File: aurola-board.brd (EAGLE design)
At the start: 86.4 x 31.8 mm, 84 parts, among them IC1 STM32F051C6T, J1 CONN_PWM, J2 CONN_TEMP, J3 CONN_FAN, J4 CONN_EC11, J5 CONN_I2C, P1 KF128-2P, Q1 600mA/40V, U1 ESP-01F, U2 BL9341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

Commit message: 完成布局
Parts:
- moved C16 0.63 mm to (30.4, 5.71)
- moved C14 0.51 mm to (30.4, 11.6)
- moved C13 0.51 mm to (30.4, 8.13)
- moved U$1 0.51 mm to (27.2, 8.00)
- moved U$2 0.38 mm to (27.2, 3.17)
- moved C15 0.25 mm to (30.4, 3.30)
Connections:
- removed net N$26: C28.+, D3.C, D4.P$1, F1.1
- new net EC_INT: IC1.42, U1.6
- net FAN_SPEED: now also IC1.13
- net VIN: now also C28.+, D3.C, D4.P$1, F1.1
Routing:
- net 3.3V: track 0.00 -> 173.9 mm, vias 0 -> 4
- net GND: track 0.00 -> 94.0 mm, vias 0 -> 78
- net FAN_SPEED: track 0.00 -> 56.4 mm, vias 0 -> 2
- net SDA: track 0.00 -> 55.6 mm, vias 0 -> 3
- net SCL: track 0.00 -> 54.7 mm, vias 0 -> 3
- net FAN_PWM: track 0.00 -> 51.1 mm, vias 0 -> 2
- net VIN: track 0.00 -> 50.7 mm, vias 0 -> 2
- net EC_INT: track 0.00 -> 47.9 mm, vias 0 -> 2
- net 12V: track 0.00 -> 37.1 mm, vias 0 -> 3
- net EC_A: track 0.00 -> 33.6 mm, vias 0 -> 2
- net RST: track 0.00 -> 30.7 mm, vias 0 -> 2
- net EC_B: track 0.00 -> 30.2 mm, vias 0 -> 2
- net EC_SW: track 0.00 -> 23.1 mm
- net TEMP_DO: track 0.00 -> 18.8 mm
- net TX: track 0.00 -> 18.8 mm
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- added copper zone on layer 1, net GND
- added copper zone on layer 16, net GND
- added copper zone on layer 1, net N$2
- added copper zone on layer 1, net N$6
- added copper zone on layer 1, net VIN

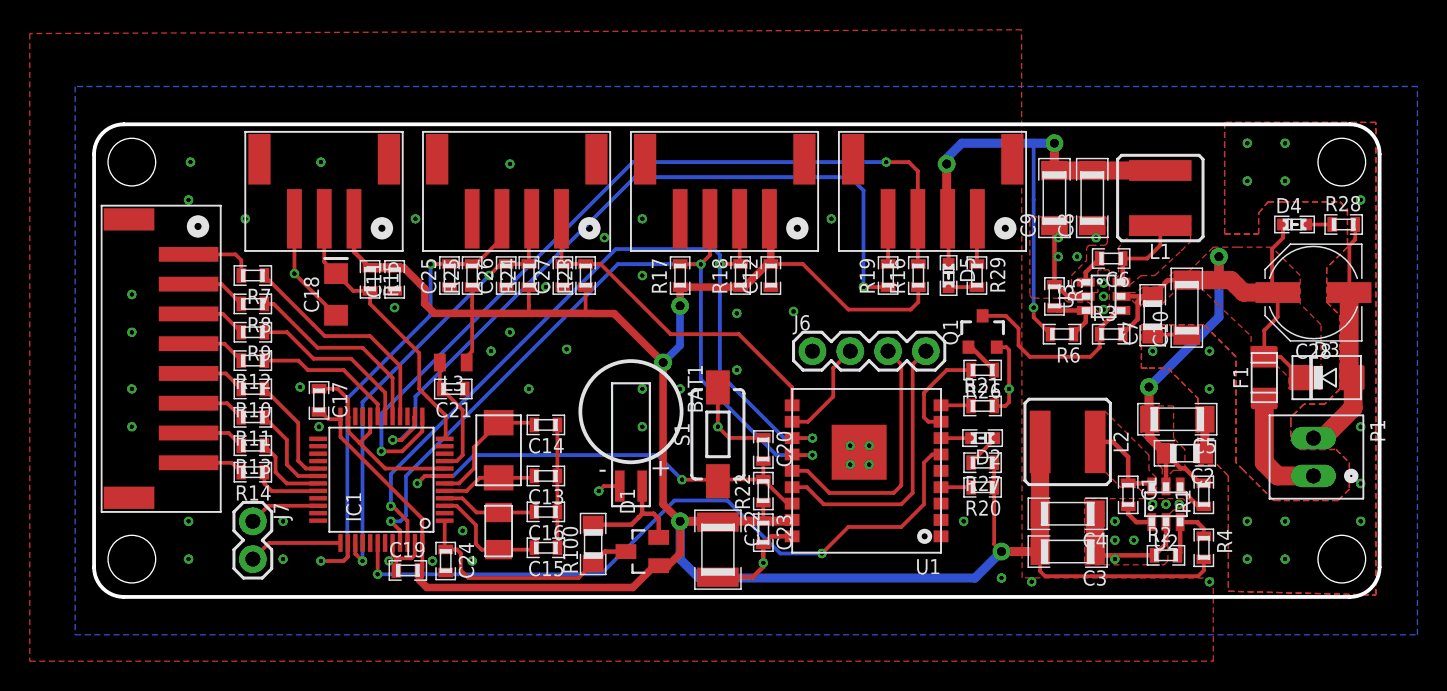
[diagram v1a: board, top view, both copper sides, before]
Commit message: 调整丝印位置
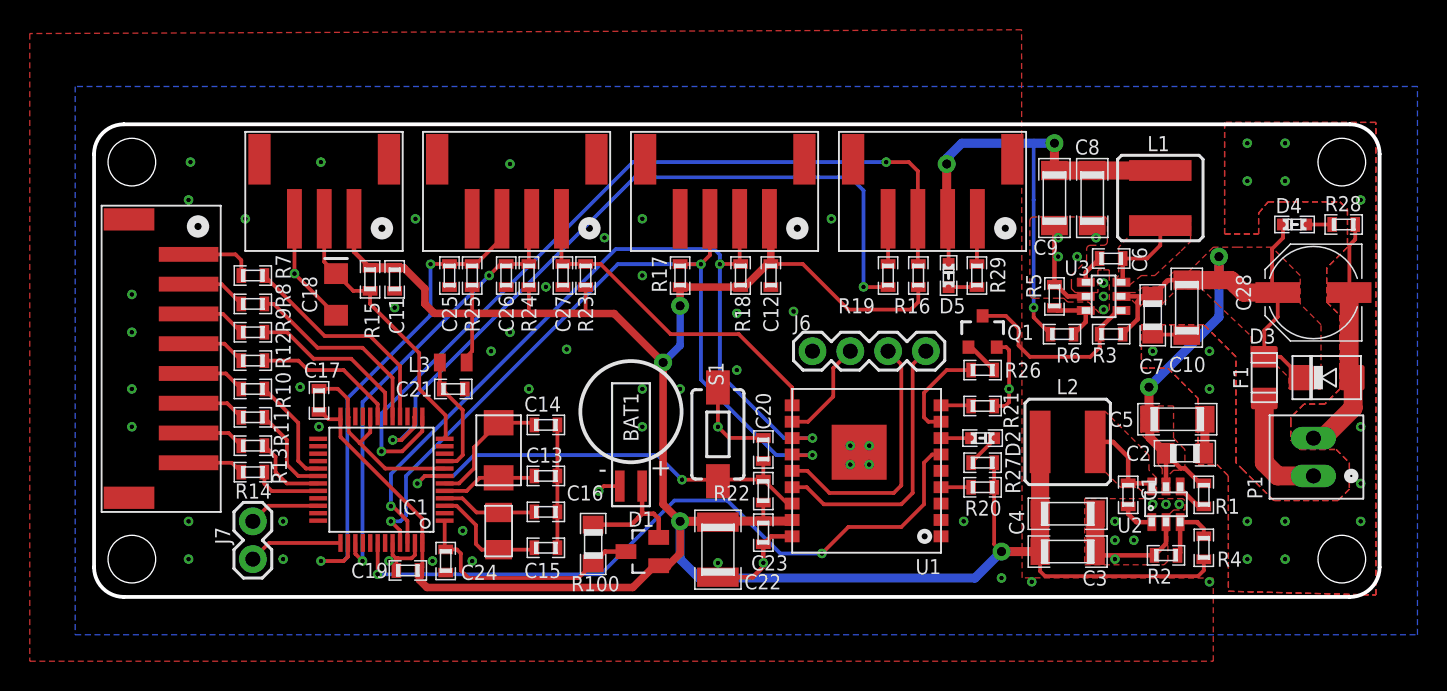
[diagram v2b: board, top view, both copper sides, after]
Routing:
- net GND: track 94.0 -> 93.6 mm, vias 78 -> 79
